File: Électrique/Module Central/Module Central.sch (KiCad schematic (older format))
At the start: 28 parts, among them J101 2.1mm X 5.5mm Barrel Connector, J102 Prog, J103 Conn_Coaxial, U101 LM2937xMP, U102 ATmega328P-AU, U103 RMF95, Y101 16MHz

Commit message: Ajout DEL témoin
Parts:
- added D105: TA, Diode_SMD:D_0805_2012Metric, symbol Device:LED
- added R106: 330, Resistor_SMD:R_0805_2012Metric, symbol Device:R
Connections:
- net 5V: now also D105.2 (A)
- net GND: now also R106.2
- new net: D105.1 (K), R106.1
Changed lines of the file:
@@
 Text Notes 6150 5050 0    50   ~ 0
 Port D garde meme numéro de pin que Arduino
-Text Notes 7950 6250 0    50   ~ 0
+Text Notes 8700 6300 0    50   ~ 0
 Témoins lumineux facultatifs
 NoConn ~ 9800 3200
@@
 Text GLabel 10350 3000 1    50   Input ~ 0
 3V3
+$Comp
+L Device:LED D105
+U 1 1 60196B8A
+P 8100 5950
+F 0 "D105" V 8139 5832 50  0000 R CNN
+F 1 "TA" V 8048 5832 50  0000 R CNN
+F 2 "Diode_SMD:D_0805_2012Metric" H 8100 5950 50  0001 C CNN
+F 3 "~" H 8100 5950 50  0001 C CNN
+	1    8100 5950
+	0    -1   -1   0
+$EndComp
+$Comp
+L Device:R R106
+U 1 1 60196B90
+P 8100 6250
+F 0 "R106" H 8170 6296 50  0000 L CNN
+F 1 "330" H 8170 6205 50  0000 L CNN
+F 2 "Resistor_SMD:R_0805_2012Metric" V 8030 6250 50  0001 C CNN
+F 3 "~" H 8100 6250 50  0001 C CNN
+	1    8100 6250
+	1    0    0    -1
+$EndComp
+Wire Wire Line
+	8100 6400 7700 6400
+Connection ~ 7700 6400
+Text GLabel 8100 5800 1    50   Input ~ 0
+5V
 $EndSCHEMATC

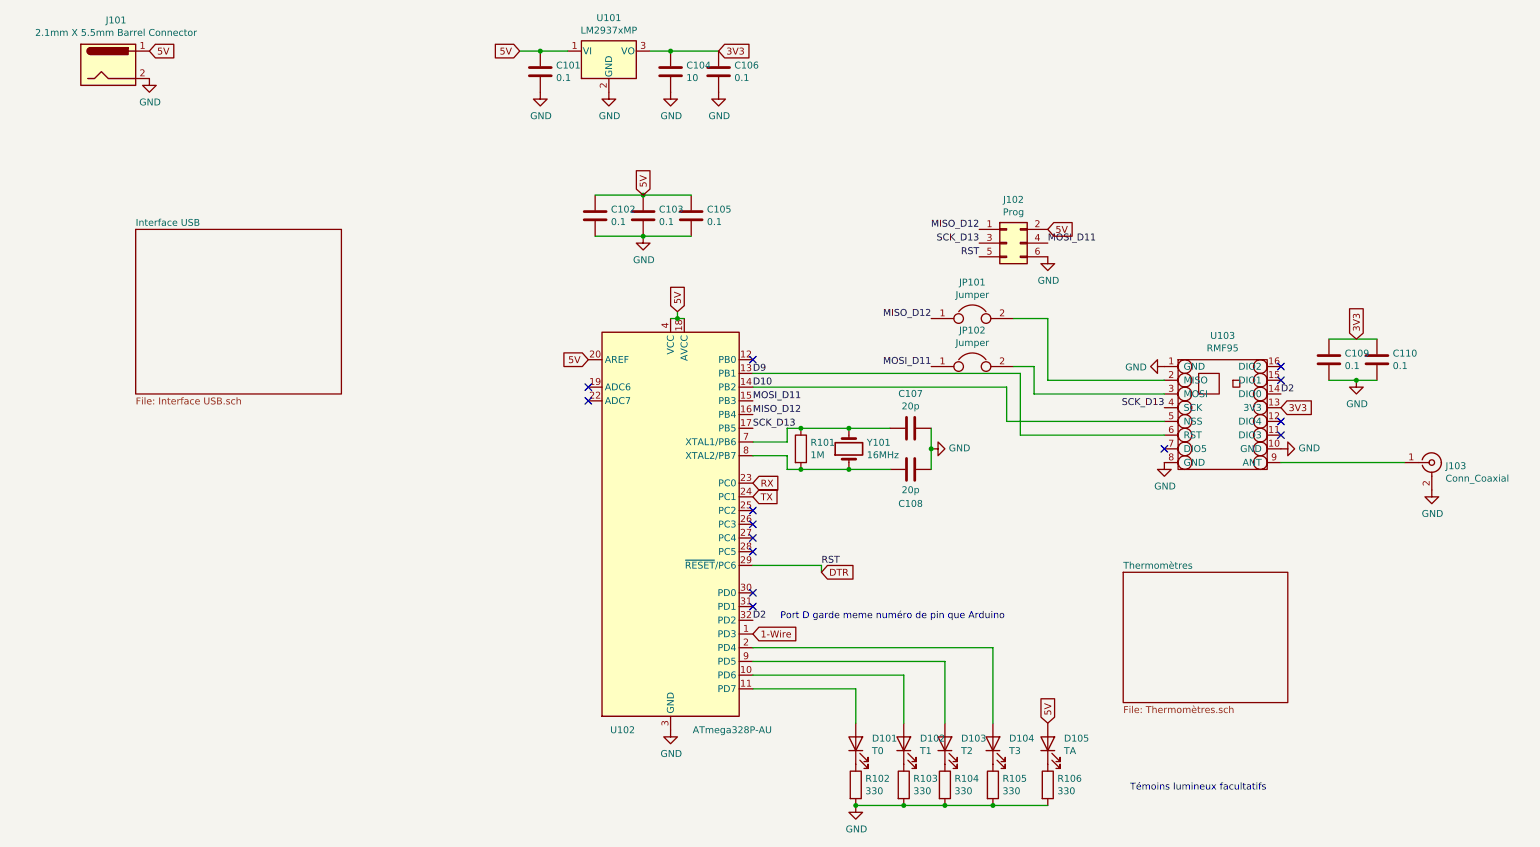
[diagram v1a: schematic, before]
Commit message: Correction des erreurs sur le schéma
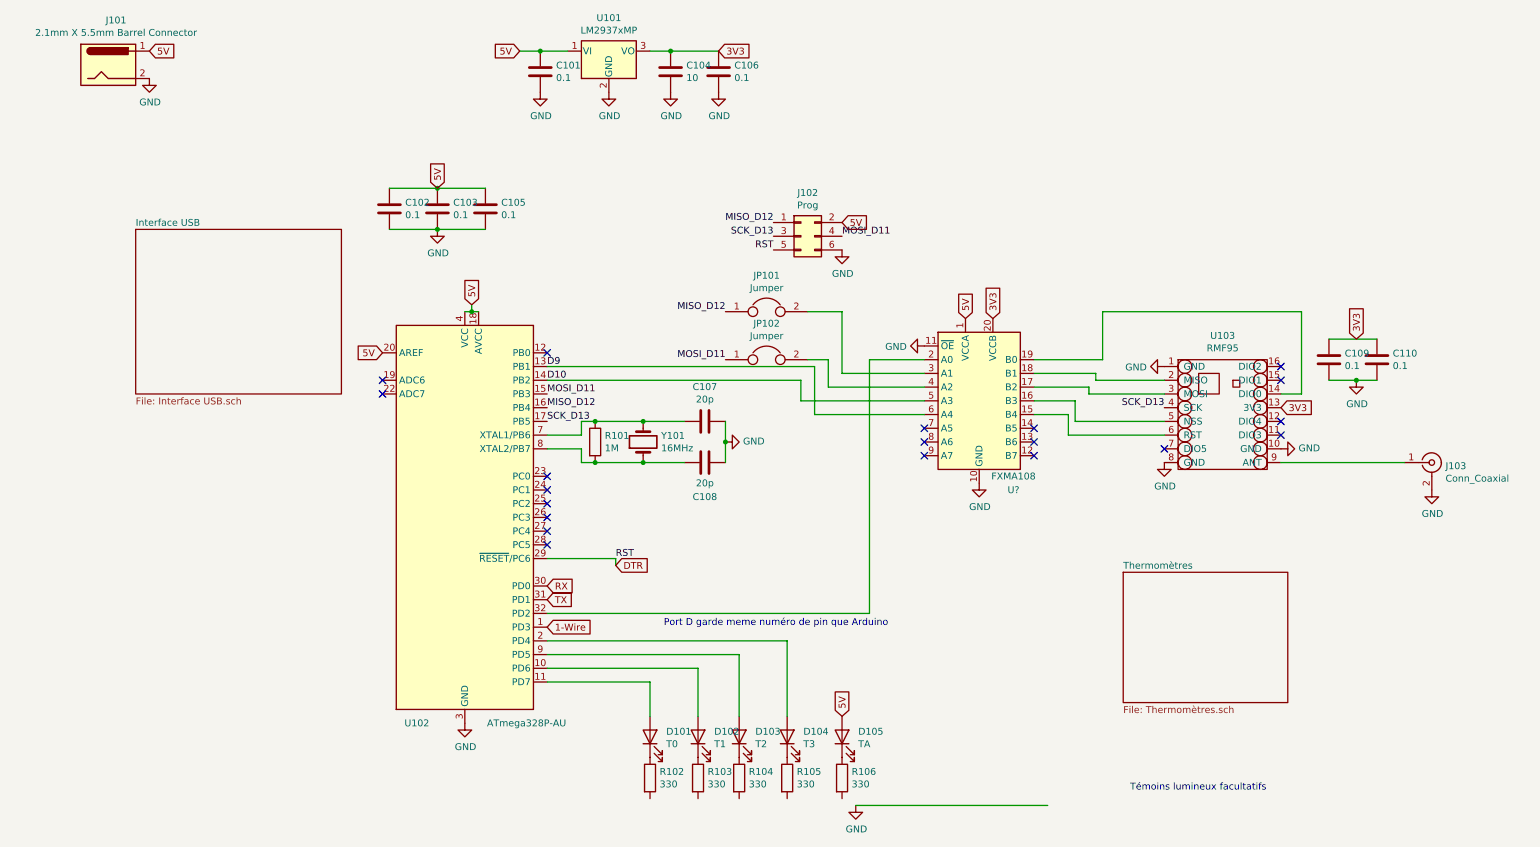
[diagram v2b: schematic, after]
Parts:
- added U?: FXMA108, Package_DFN_QFN:WQFN-20-1EP_2.5x4.5mm_P0.5mm_EP1x2.9mm, symbol Logic_LevelTranslator:FXMA108
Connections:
- net 3V3: now also U?.20 (VCCB)
- net 5V: now also U?.1 (VCCA)
- net D10: now also U?.5 (A3); no longer U103.5 (NSS)
- net D9: now also U?.6 (A4); no longer U103.6 (RST)
- net GND: now also U?.10 (GND), U?.11 (~OE); no longer R102.2, R103.2, R104.2, R105.2, R106.2
- net RX: now also U102.30 (PD0); no longer U102.23 (PC0)
- net TX: now also U102.31 (PD1); no longer U102.24 (PC1)
- net at U103.2 (MISO): now also U?.18 (B1); no longer JP101.2
- net at U103.3 (MOSI): now also U?.17 (B2); no longer JP102.2
- net D2: no longer names the net of U102.32 (PD2)
- net D2: now also U?.2 (A0); no longer U103.14 (DIO0)
- new net: U103.14 (DIO0), U?.19 (B0)
- new net: U103.5 (NSS), U?.16 (B3)
- new net: U103.6 (RST), U?.15 (B4)
- new net: JP101.2, U?.3 (A1)
- new net: JP102.2, U?.4 (A2)
- no-connect marks 14 -> 20
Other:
- moved on the sheet: C102, C103, C105, C107, C108, D101, D102, D103, D104, D105, J102, JP101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

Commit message: Modification PCB prete à faire
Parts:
- gave numbers to parts that had none: 1
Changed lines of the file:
@@
 	6800 3150 7200 3150
 $Comp
-L Logic_LevelTranslator:FXMA108 U?
+L Logic_LevelTranslator:FXMA108 U104
 U 1 1 60399B14
 P 7600 3450
-F 0 "U?" H 7850 2800 50  0000 C CNN
+F 0 "U104" H 7850 2800 50  0000 C CNN
 F 1 "FXMA108" H 7850 2900 50  0000 C CNN
 F 2 "Package_DFN_QFN:WQFN-20-1EP_2.5x4.5mm_P0.5mm_EP1x2.9mm" H 7600 2750 50  0001 C CNN
@@
 NoConn ~ 8000 3850
 $Comp
-L power:GND #PWR?
+L power:GND #PWR0116
 U 1 1 603B0F0C
 P 7200 3050
-F 0 "#PWR?" H 7200 2800 50  0001 C CNN
+F 0 "#PWR0116" H 7200 2800 50  0001 C CNN
 F 1 "GND" V 7205 2922 50  0000 R CNN
 F 2 "" H 7200 3050 50  0001 C CNN
@@
 3V3
 $Comp
-L power:GND #PWR?
+L power:GND #PWR0117
 U 1 1 603B1E4F
 P 7600 4050
-F 0 "#PWR?" H 7600 3800 50  0001 C CNN
+F 0 "#PWR0117" H 7600 3800 50  0001 C CNN
 F 1 "GND" H 7605 3877 50  0000 C CNN
 F 2 "" H 7600 4050 50  0001 C CNN

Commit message: oups
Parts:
- U103: symbol Module-Central-rescue:RMF95-ProjetChambreFroide -> Module-Central-rescue:RMF95-ProjetChambreFroide-Module-Central-rescue
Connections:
- net GND: now also R102.2, R103.2, R104.2, R105.2, R106.2
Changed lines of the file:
@@
 	4800 3900 4700 3900
 $Comp
-L Module-Central-rescue:RMF95-ProjetChambreFroide U103
+L Module-Central-rescue:RMF95-ProjetChambreFroide-Module-Central-rescue U103
 U 1 1 600621C7
 P 9350 3100
@@
 L power:GND #PWR0108
 U 1 1 600BD4CB
-P 6700 6400
-F 0 "#PWR0108" H 6700 6150 50  0001 C CNN
-F 1 "GND" H 6705 6227 50  0000 C CNN
-F 2 "" H 6700 6400 50  0001 C CNN
-F 3 "" H 6700 6400 50  0001 C CNN
-	1    6700 6400
+P 5200 6350
+F 0 "#PWR0108" H 5200 6100 50  0001 C CNN
+F 1 "GND" H 5205 6177 50  0000 C CNN
+F 2 "" H 5200 6350 50  0001 C CNN
+F 3 "" H 5200 6350 50  0001 C CNN
+	1    5200 6350
 	1    0    0    -1
 $EndComp
@@
 NoConn ~ 4450 4100
 Wire Wire Line
-	6700 6400 8100 6400
+	5200 6350 5550 6350
 Wire Wire Line
 	8250 3550 8250 3700
@@
 	1    0    0    -1
 $EndComp
+Connection ~ 5200 6350
+Connection ~ 5550 6350
+Wire Wire Line
+	5550 6350 5850 6350
+Connection ~ 5850 6350
+Wire Wire Line
+	5850 6350 6200 6350
+Connection ~ 6200 6350
+Wire Wire Line
+	6200 6350 6600 6350
 $EndSCHEMATC

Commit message: PCB modifié
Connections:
- net SCK_D13: now also U104.7 (A5); no longer U103.4 (SCK)
- net at U104.14 (B5): now also U103.4 (SCK)
- no-connect marks 20 -> 18
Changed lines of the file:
@@
 	1    0    0    -1
 $EndComp
-Text Label 4450 3600 0    50   ~ 0
-SCK_D13
 Wire Wire Line
 	4450 3300 6300 3300
@@
 Text Label 4950 4600 0    50   ~ 0
 RST
-Text Label 8950 3500 2    50   ~ 0
-SCK_D13
 $Comp
 L Device:Jumper JP101
@@
 	1    0    0    -1
 $EndComp
-NoConn ~ 7200 3650
 NoConn ~ 7200 3750
 NoConn ~ 7200 3850
@@
 Wire Wire Line
 	8250 3550 8000 3550
-NoConn ~ 8000 3650
 NoConn ~ 8000 3750
 NoConn ~ 8000 3850
@@
 Wire Wire Line
 	6200 6350 6600 6350
+Text Label 4450 3600 0    50   ~ 0
+SCK_D13
+Text Label 7200 3650 2    50   ~ 0
+SCK_D13
+Wire Wire Line
+	8000 3650 8450 3650
+Wire Wire Line
+	8450 3650 8450 3500
+Wire Wire Line
+	8450 3500 8950 3500
 $EndSCHEMATC
